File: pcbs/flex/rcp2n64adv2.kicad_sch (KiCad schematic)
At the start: 18 parts, among them J1 Conn_01x01, J2 Conn_01x01, J3 Conn_01x01, J3.1 Conn_01x01, J4 Conn_01x01, J5 Conn_01x01, J6 Conn_01x30, U1 74LVC1G17, X1 n64_rcp_vid_aud_out_no_3v3_con, X2 Conn_01x01

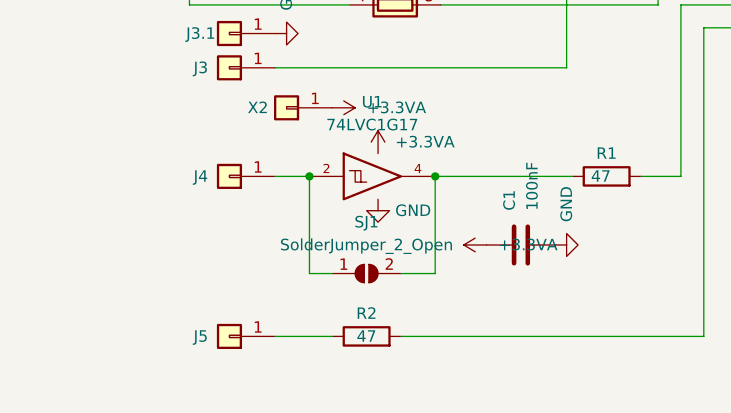
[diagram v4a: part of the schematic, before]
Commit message: Update flex-PCB: - move buffer IC to resistor array area of PCB (not on arms anymore) - add pads as backup if arms get ripped off
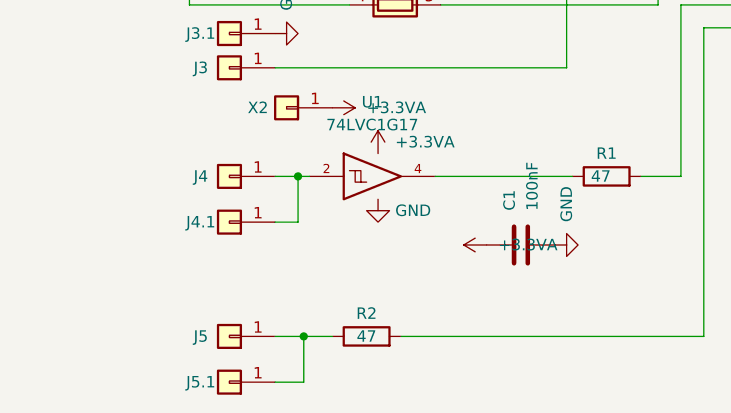
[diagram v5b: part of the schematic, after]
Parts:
- removed SJ1: SolderJumper_2_Open, Jumper:SolderJumper-2_P1.3mm_Open_RoundedPad1.0x1.5mm, symbol Jumper:SolderJumper_2_Open
- added J4.1, J5.1: Conn_01x01, TestPoint:TestPoint_Pad_D1.5mm, symbol Connector_Generic:Conn_01x01
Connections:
- net at J5.1 (Pin_1), R2.1: now also J5.1.1 (Pin_1)
- net at J4.1 (Pin_1), U1.2: now also J4.1.1 (Pin_1)
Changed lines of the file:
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@@
   (title_block
     (title "RCP2N64Adv2")
-    (rev "v20220903")
+    (rev "v20231105")
     (company "Peter 'borti4938' Bartmann")
-    (comment 1 "Schematic and PCB (c) 2021, 2022 by Peter Bartmann")
+    (comment 1 "Schematic and PCB (c) 2021-2023 by Peter Bartmann")
     (comment 2 "Licensed under CERN-OHL-W v2")
   )
-  (junction (at 77.47 144.78) (diameter 0) (color 0 0 0 0)
-  )
   (junction (at 92.075 80.01) (diameter 0) (color 0 0 0 0)
   )
   (junction (at 92.075 113.03) (diameter 0) (color 0 0 0 0)
   )
-  (junction (at 91.44 144.78) (diameter 0) (color 0 0 0 0)
-  )
   (junction (at 92.075 107.95) (diameter 0) (color 0 0 0 0)
   )
+  (junction (at 76.835 162.56) (diameter 0) (color 0 0 0 0)
+  )
+  (junction (at 76.2 144.78) (diameter 0) (color 0 0 0 0)
+  )
   (junction (at 92.075 120.65) (diameter 0) (color 0 0 0 0)
   )
@@
     (stroke (width 0) (type default) (color 0 0 0 0))
   )
-  (wire (pts (xy 87.63 155.575) (xy 91.44 155.575))
-    (stroke (width 0) (type default) (color 0 0 0 0))
-  )
   (wire (pts (xy 116.205 120.65) (xy 131.445 120.65))
     (stroke (width 0) (type default) (color 0 0 0 0))
@@
     (stroke (width 0) (type default) (color 0 0 0 0))
   )
+  (wire (pts (xy 76.2 144.78) (xy 77.47 144.78))
+    (stroke (width 0) (type default) (color 0 0 0 0))
+  )
   (wire (pts (xy 73.66 132.715) (xy 106.045 132.715))
     (stroke (width 0) (type default) (color 0 0 0 0))
@@
     (stroke (width 0) (type default) (color 0 0 0 0))
   )
-  (wire (pts (xy 73.66 162.56) (xy 80.01 162.56))
+  (wire (pts (xy 73.66 162.56) (xy 76.835 162.56))
     (stroke (width 0) (type default) (color 0 0 0 0))
   )
@@
     (stroke (width 0) (type default) (color 0 0 0 0))
   )
-  (wire (pts (xy 77.47 144.78) (xy 77.47 155.575))
-    (stroke (width 0) (type default) (color 0 0 0 0))
-  )
   (wire (pts (xy 104.14 107.95) (xy 104.14 110.49))
     (stroke (width 0) (type default) (color 0 0 0 0))
@@
     (stroke (width 0) (type default) (color 0 0 0 0))
   )
-  (wire (pts (xy 77.47 155.575) (xy 80.01 155.575))
+  (wire (pts (xy 73.66 167.64) (xy 76.835 167.64))
     (stroke (width 0) (type default) (color 0 0 0 0))
   )
@@
     (stroke (width 0) (type default) (color 0 0 0 0))
   )
+  (wire (pts (xy 76.2 149.86) (xy 76.2 144.78))
+    (stroke (width 0) (type default) (color 0 0 0 0))
+  )
   (wire (pts (xy 118.745 100.33) (xy 118.745 97.79))
     (stroke (width 0) (type default) (color 0 0 0 0))
   )
+  (wire (pts (xy 73.66 149.86) (xy 76.2 149.86))
+    (stroke (width 0) (type default) (color 0 0 0 0))
+  )
   (wire (pts (xy 92.075 105.41) (xy 111.125 105.41))
     (stroke (width 0) (type default) (color 0 0 0 0))
@@
     (stroke (width 0) (type default) (color 0 0 0 0))
   )
-  (wire (pts (xy 73.66 144.78) (xy 77.47 144.78))
+  (wire (pts (xy 73.66 144.78) (xy 76.2 144.78))
     (stroke (width 0) (type default) (color 0 0 0 0))
   )
@@
     (stroke (width 0) (type default) (color 0 0 0 0))
   )
-  (wire (pts (xy 91.44 155.575) (xy 91.44 144.78))
-    (stroke (width 0) (type default) (color 0 0 0 0))
-  )
   (wire (pts (xy 111.125 113.03) (xy 131.445 113.03))
     (stroke (width 0) (type default) (color 0 0 0 0))
@@
     (stroke (width 0) (type default) (color 0 0 0 0))
   )
+  (wire (pts (xy 76.835 167.64) (xy 76.835 162.56))
+    (stroke (width 0) (type default) (color 0 0 0 0))
+  )
   (wire (pts (xy 106.045 110.49) (xy 131.445 110.49))
     (stroke (width 0) (type default) (color 0 0 0 0))
@@
   )
   (wire (pts (xy 111.76 92.71) (xy 111.76 90.17))
+    (stroke (width 0) (type default) (color 0 0 0 0))
+  )
+  (wire (pts (xy 76.835 162.56) (xy 80.01 162.56))
     (stroke (width 0) (type default) (color 0 0 0 0))
   )
@@
     (pin "1")
   )
+  (symbol (lib_id "Connector_Generic:Conn_01x01") (at 68.58 149.86 180) (unit 1)
+    (in_bom no) (on_board yes)
+    (property "Reference" "J4.1" (id 0) (at 65.405 149.86 0))
+    (property "Value" "Conn_01x01" (id 1) (at 68.58 146.05 0)
+      (effects (font (size 1.27 1.27)) hide)
+    )
+    (property "Footprint" "TestPoint:TestPoint_Pad_D1.5mm" (id 2) (at 68.58 149.86 0)
+      (effects (font (size 1.27 1.27)) hide)
+    )
+    (property "Datasheet" "~" (id 3) (at 68.58 149.86 0)
+      (effects (font (size 1.27 1.27)) hide)
+    )
+    (pin "1")
+  )
   (symbol (lib_id "power:GND") (at 59.055 90.17 90) (unit 1)
     (in_bom yes) (on_board yes) (fields_autoplaced)
@@
     )
     (pin "1")
-  )
-  (symbol (lib_id "Jumper:SolderJumper_2_Open") (at 83.82 155.575 0) (unit 1)
-    (in_bom no) (on_board yes) (fields_autoplaced)
-    (property "Reference" "SJ1" (id 0) (at 83.82 149.86 0))
-    (property "Value" "SolderJumper_2_Open" (id 1) (at 83.82 152.4 0))
-    (property "Footprint" "Jumper:SolderJumper-2_P1.3mm_Open_RoundedPad1.0x1.5mm" (id 2) (at 83.82 155.575 0)
-      (effects (font (size 1.27 1.27)) hide)
-    )
-    (property "Datasheet" "~" (id 3) (at 83.82 155.575 0)
-      (effects (font (size 1.27 1.27)) hide)
-    )
-    (pin "1")
-    (pin "2")
   )
   (symbol (lib_id "power:+3.3VA") (at 97.155 152.4 90) (unit 1)
@@
     (pin "1")
   )
+  (symbol (lib_id "Connector_Generic:Conn_01x01") (at 68.58 167.64 180) (unit 1)
+    (in_bom no) (on_board yes)
+    (property "Reference" "J5.1" (id 0) (at 65.405 167.64 0))
+    (property "Value" "Conn_01x01" (id 1) (at 68.58 163.83 0)
+      (effects (font (size 1.27 1.27)) hide)
+    )
+    (property "Footprint" "TestPoint:TestPoint_Pad_D1.5mm" (id 2) (at 68.58 167.64 0)
+      (effects (font (size 1.27 1.27)) hide)
+    )
+    (property "Datasheet" "~" (id 3) (at 68.58 167.64 0)
+      (effects (font (size 1.27 1.27)) hide)
+    )
+    (pin "1")
+  )
   (symbol (lib_id "Connector_Generic:Conn_01x01") (at 74.93 137.16 180) (unit 1)
     (in_bom no) (on_board yes)
@@
       (reference "J4") (unit 1) (value "Conn_01x01") (footprint "smd_edge_con:medium")
     )
+    (path "/77ca4237-c937-453c-b19e-29e4851879e4"
+      (reference "J4.1") (unit 1) (value "Conn_01x01") (footprint "TestPoint:TestPoint_Pad_D1.5mm")
+    )
     (path "/a7824739-d758-4dec-a7bc-74485ea7aca8"
       (reference "J5") (unit 1) (value "Conn_01x01") (footprint "smd_edge_con:medium")
     )
+    (path "/edf7c234-9098-4f7a-b72d-acdc3d388418"
+      (reference "J5.1") (unit 1) (value "Conn_01x01") (footprint "TestPoint:TestPoint_Pad_D1.5mm")
+    )
     (path "/b98c90dc-edc3-49d3-be61-1c82a69b8385"
       (reference "J6") (unit 1) (value "Conn_01x30") (footprint "ffc_cable_edge:EDGE-FH12-30S-0.5SH")
@@
       (reference "RN4") (unit 1) (value "R_Pack04") (footprint "Resistor_SMD:R_Array_Convex_4x0603")
     )
-    (path "/8fb41a33-8fc0-4a8d-8ae7-94e234723f48"
-      (reference "SJ1") (unit 1) (value "SolderJumper_2_Open") (footprint "Jumper:SolderJumper-2_P1.3mm_Open_RoundedPad1.0x1.5mm")
-    )
     (path "/42e45e2c-9977-480b-a863-c6494dbed837"
